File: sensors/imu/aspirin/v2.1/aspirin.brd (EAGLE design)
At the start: 18.8 x 15.5 mm, 23 parts, among them IC1 LP2992, IC2 MS5611, IC3 >4KBIT SERIAL EEPROM HALF PRO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, U1 HMC5883, U2 MPU-6000

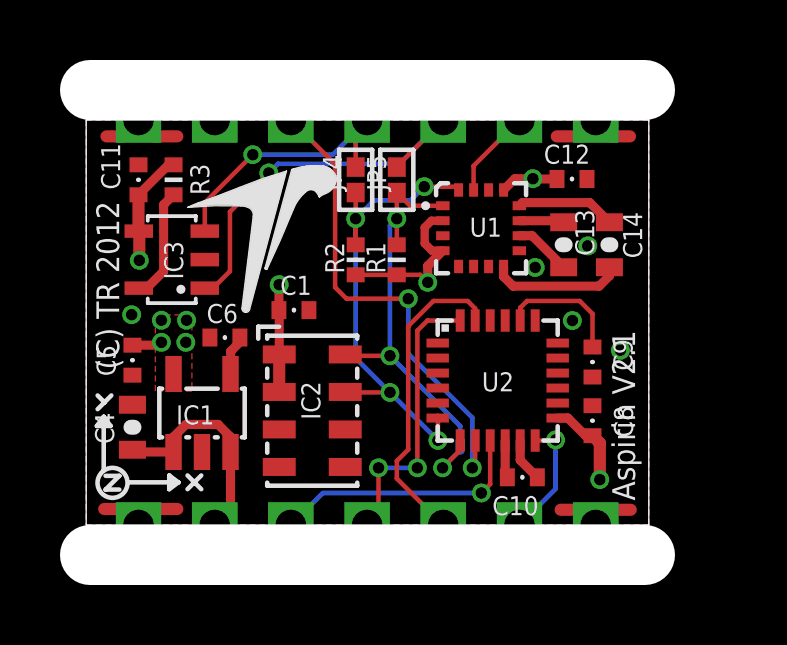
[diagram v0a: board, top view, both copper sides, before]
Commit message: Some minor cleanups and touchups. Renamed signal silkscreen legend's to better reflect reality.
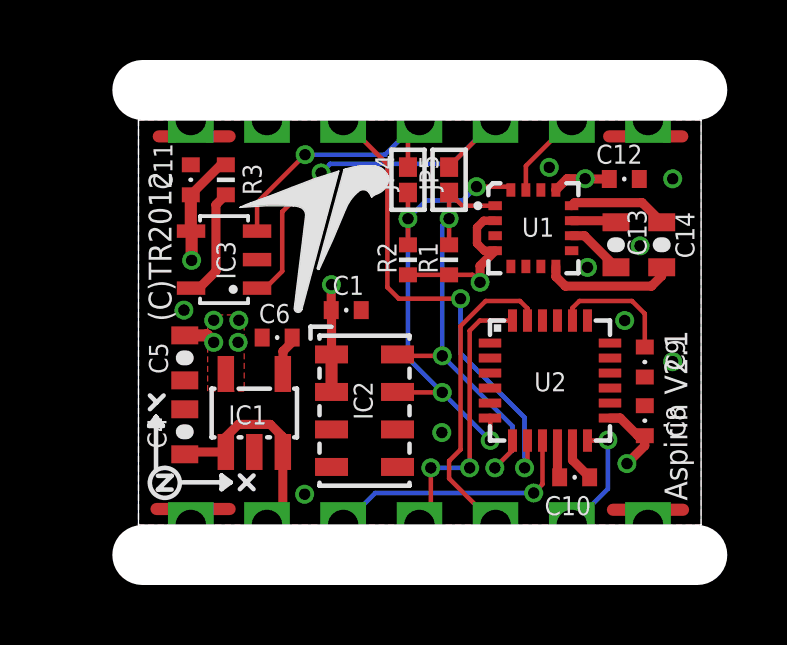
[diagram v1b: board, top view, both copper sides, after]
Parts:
- C5: device pel_dipol_comp:0402-CAP -> pel_dipol_comp:0603-CAP
- moved C4 1.75 mm to (1.54, 3.11)
- moved C5 1.74 mm to (1.54, 5.57)
- moved C10 1.74 mm to (14.5, 1.59)
- moved C12 1.74 mm to (16.2, 11.5)
- moved C13 1.74 mm to (15.9, 9.34)
- moved IC2 1.74 mm to (7.53, 3.81)
- moved JP4 1.74 mm to (8.98, 11.5)
- moved R2 1.74 mm to (8.98, 8.84)
- moved U$1 1.74 mm to (5.86, 9.53)
- moved ASP1 1.74 mm to (1.74, 0.00)
- moved C11 1.74 mm to (1.74, 11.5)
- moved R3 1.74 mm to (2.91, 11.5)
- moved IC3 1.74 mm to (2.85, 8.85)
- moved C1 1.74 mm to (6.92, 7.16)
- moved C14 1.74 mm to (17.4, 9.34)
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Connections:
- removed net GYRO_INT: ASP1.9, U1.15
- new net MPU_INT: ASP1.6, U2.12
- net MAG_INT: now also ASP1.9, U1.15; no longer ASP1.6, U2.12
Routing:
- net MPU_INT: track 0.00 -> 4.02 mm, vias 0 -> 1
- net GYRO_INT: track 2.97 -> 0.00 mm
- net MAG_INT: track 4.02 -> 2.97 mm, vias 1 -> 0
- net GND: vias 5 -> 9
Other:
- board text added: "(C)TR2012"
- board text added: "MPU_CS"
- board text added: "MPU_INT"
- board text added: "RESV"
- board text removed: "(C) 2011 Joby Robotics <info@jobyrobotics.com>"
- board text removed: "(C) TR 2012"
- board text removed: "ACC_CS"
- board text removed: "ACC_INT"
- board text removed: "GYRO_INT"

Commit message: Renamed ACC_CS to MPU_CS and changed panel to 3x3.
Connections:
- net ACC_CS renamed MPU_CS
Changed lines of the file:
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@@
 <wire x1="10.7937" y1="10.6426" x2="10.3539" y2="11.0824" width="0.1524" layer="1"/>
 </signal>
-<signal name="ACC_CS">
+<signal name="MPU_CS">
 <contactref element="U2" pad="8"/>
 <contactref element="ASP1" pad="12"/>

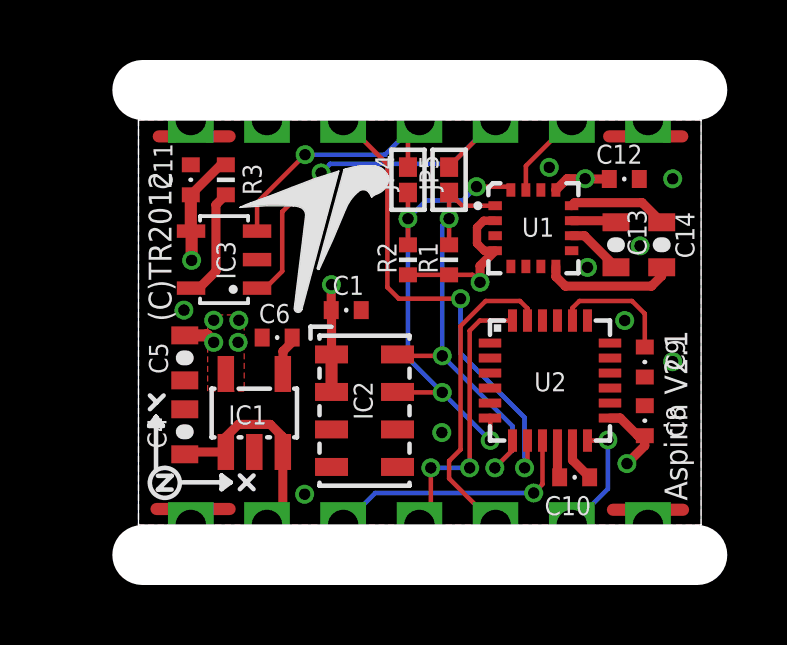
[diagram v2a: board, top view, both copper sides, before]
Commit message: Changed via size to 0.4mm.
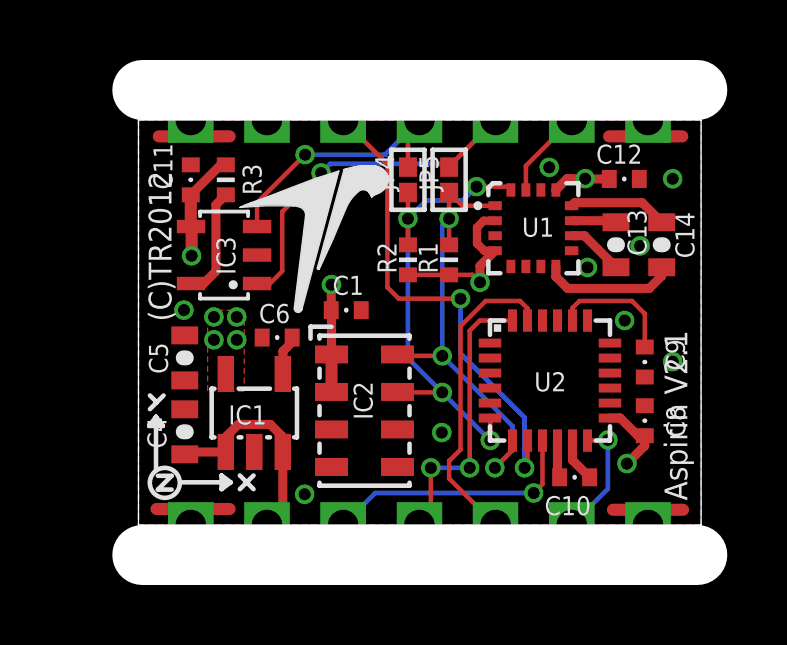
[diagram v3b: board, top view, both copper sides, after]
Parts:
- moved IC3 0.15 mm to (2.85, 9.00)
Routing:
- net +3V3: track 18.7 -> 17.4 mm

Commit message: Minor final fixes before going into assembly.
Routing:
- net +3V3: track 17.4 -> 18.6 mm
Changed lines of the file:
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@@
 <layers>
 <layer number="1" name="Top" color="4" fill="1" visible="yes" active="yes"/>
-<layer number="2" name="Route2" color="1" fill="3" visible="yes" active="yes"/>
+<layer number="2" name="Route2" color="1" fill="3" visible="no" active="yes"/>
 <layer number="3" name="Route3" color="4" fill="3" visible="no" active="no"/>
 <layer number="4" name="Route4" color="1" fill="4" visible="no" active="no"/>
@@
 <layer number="13" name="Route13" color="4" fill="5" visible="no" active="no"/>
 <layer number="14" name="Route14" color="1" fill="6" visible="no" active="no"/>
-<layer number="15" name="Route15" color="4" fill="6" visible="yes" active="yes"/>
+<layer number="15" name="Route15" color="4" fill="6" visible="no" active="yes"/>
 <layer number="16" name="Bottom" color="1" fill="1" visible="yes" active="yes"/>
 <layer number="17" name="Pads" color="2" fill="1" visible="yes" active="yes"/>
@@
 <circle x="0.878" y="1.4046" radius="0.5" width="0.1524" layer="21"/>
 <circle x="12.0049" y="11.0236" radius="0.27" width="0.1524" layer="51"/>
-<circle x="1.5147" y="7.0104" radius="0.1778" width="0.3556" layer="29"/>
+<circle x="1.5147" y="7.239" radius="0.1778" width="0.3556" layer="29"/>
 <text x="18.2965" y="0.8151" size="0.762" layer="21" font="vector" ratio="20" rot="R90">Aspirin V2.1</text>
 <text x="1.1007" y="6.7841" size="0.762" layer="21" font="vector" ratio="20" rot="R90">(C)TR2012</text>
@@
 <attribute name="VALUE" x="4.7345" y="6.31" size="0.8128" layer="27" font="vector" ratio="16" rot="R270"/>
 <attribute name="PARTNO" value="sensr-qfn-8-baro" x="7.5345" y="3.81" size="1.778" layer="27" display="off"/>
+<attribute name="DNP" value="T" x="7.5345" y="3.81" size="1.778" layer="27" display="off"/>
 </element>
 <element name="C1" library="pel_dipol_comp" package="0402-CAP" value="100n" x="6.9249" y="7.1628" smashed="yes">
@@
 <attribute name="VALUE" x="5.7819" y="5.8674" size="0.635" layer="27" font="vector" ratio="16"/>
 <attribute name="PARTNO" value="cap-cer-0402-100n" x="6.9249" y="7.1628" size="1.778" layer="27" display="off"/>
+<attribute name="DNP" value="T" x="6.9249" y="7.1628" size="1.778" layer="27" display="off"/>
 </element>
 <element name="R1" library="pel_dipol_comp" package="0402-RES" value="4k7" x="10.3539" y="8.8392" smashed="yes" rot="R90">
@@
 <via x="16.7198" y="9.3032" extent="1-16" drill="0.4"/>
 <via x="14.9672" y="8.5854" extent="1-16" drill="0.4"/>
-<via x="1.5147" y="7.1628" extent="1-16" drill="0.4"/>
+<via x="1.5147" y="7.239" extent="1-16" drill="0.4"/>
 <via x="16.2064" y="6.8158" extent="1-16" drill="0.4"/>
 <polygon width="0.2032" layer="1" rank="6">
@@
 <wire x1="16.8764" y1="2.9768" x2="16.8764" y2="2.6413" width="0.3048" layer="1"/>
 <wire x1="16.8764" y1="2.6413" x2="16.2819" y2="2.0468" width="0.3048" layer="1"/>
-<wire x1="2.5146" y1="6.1722" x2="1.5424" y2="6.3202" width="0" layer="19" extent="1-1"/>
+<wire x1="1.5424" y1="6.3202" x2="2.5146" y2="6.3202" width="0.4064" layer="1"/>
+<wire x1="2.5146" y1="6.3202" x2="2.5146" y2="6.1722" width="0.4064" layer="1"/>
 </signal>
 <signal name="N$1">

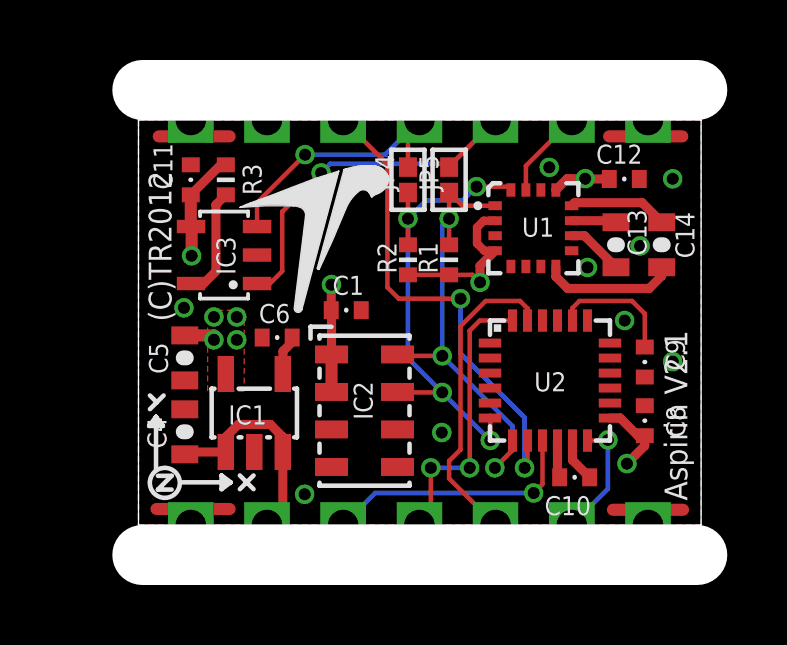
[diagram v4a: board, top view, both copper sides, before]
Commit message: Fixed the corner pin intended for GYRO_CS to be disconnected from ground and labeled RESV on the pcb.
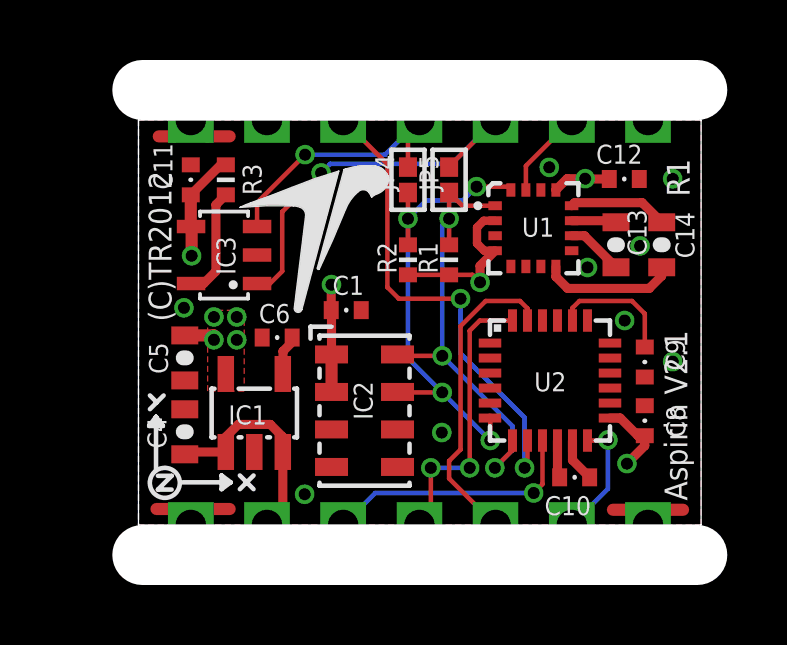
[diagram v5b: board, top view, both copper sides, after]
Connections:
- net GND: no longer ASP1.8
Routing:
- net GND: track 14.4 -> 11.5 mm
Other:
- board text added: "R1"
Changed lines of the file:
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@@
 <?xml version="1.0" encoding="utf-8"?>
 <!DOCTYPE eagle SYSTEM "eagle.dtd">
-<eagle version="6.1">
+<eagle version="6.2">
 <drawing>
 <settings>
@@
 <text x="1.4554" y="0.9328" size="0.635" layer="22" font="vector" ratio="16" rot="MR90">GND</text>
 <text x="16.6446" y="0.9328" size="0.635" layer="22" font="vector" ratio="16" rot="MR90">GND</text>
-<text x="17.3406" y="12.6054" size="0.635" layer="22" font="vector" ratio="16" rot="MR270">GND</text>
+<text x="17.3406" y="12.6054" size="0.635" layer="22" font="vector" ratio="16" rot="MR270">RESV</text>
 <text x="2.0498" y="12.5292" size="0.635" layer="22" font="vector" ratio="16" rot="MR270">GND</text>
 <text x="4.5644" y="12.6562" size="0.635" layer="22" font="vector" ratio="16" rot="MR270">RESV</text>
@@
 <circle x="1.132" y="1.5062" radius="0.5" width="0.1524" layer="51"/>
 <rectangle x1="7.9155" y1="4.953" x2="7.9917" y2="5.1816" layer="41"/>
+<text x="18.3727" y="10.9497" size="0.762" layer="21" font="vector" ratio="20" rot="R90">R1</text>
 </plain>
 <attributes>
@@
 <contactref element="ASP1" pad="7"/>
 <contactref element="ASP1" pad="14"/>
-<contactref element="ASP1" pad="8"/>
 <contactref element="IC2" pad="3"/>
 <contactref element="C1" pad="P$2"/>
 <contactref element="IC2" pad="4"/>
 <contactref element="IC2" pad="5"/>
-<wire x1="16.9833" y1="13.4874" x2="16.9833" y2="13.5" width="0.4064" layer="1"/>
 <wire x1="1.2099" y1="0.5334" x2="0.6003" y2="0.5334" width="0.4064" layer="1"/>
 <wire x1="1.7433" y1="0" x2="1.2099" y2="0.5334" width="0.4064" layer="1"/>
@@
 <wire x1="1.2099" y1="12.954" x2="0.6765" y2="12.954" width="0.4064" layer="1"/>
 <wire x1="1.7433" y1="13.4874" x2="1.2099" y2="12.954" width="0.4064" layer="1"/>
-<wire x1="17.5167" y1="12.954" x2="18.1263" y2="12.954" width="0.4064" layer="1"/>
-<wire x1="16.9833" y1="13.4874" x2="17.5167" y2="12.954" width="0.4064" layer="1"/>
-<wire x1="16.4499" y1="12.954" x2="15.6879" y2="12.954" width="0.4064" layer="1"/>
-<wire x1="16.4499" y1="12.954" x2="16.9833" y2="13.4874" width="0.4064" layer="1"/>
 <wire x1="1.7433" y1="13.5" x2="1.7433" y2="13.4874" width="0.1524" layer="1"/>
 <wire x1="15.8654" y1="10.1426" x2="15.9166" y2="10.0914" width="0.3048" layer="1"/>
